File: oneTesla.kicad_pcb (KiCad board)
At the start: 2 copper layers, 106 x 106 mm, 48 parts, among them IC1 74HCT14, IC2 74HCT74, IC3 UCC37321P, IC4 UCC37321P, IC6 78L05, J1 IEC C6, J110 Jumper 110V, J2 PE/CHASSIS, P1 PRIMARIO A, P2 PRIMARIO B, Q1 FGA60N65SMD, Q2 FGA60N65SMD, T1 1:1:1, T3 1:300

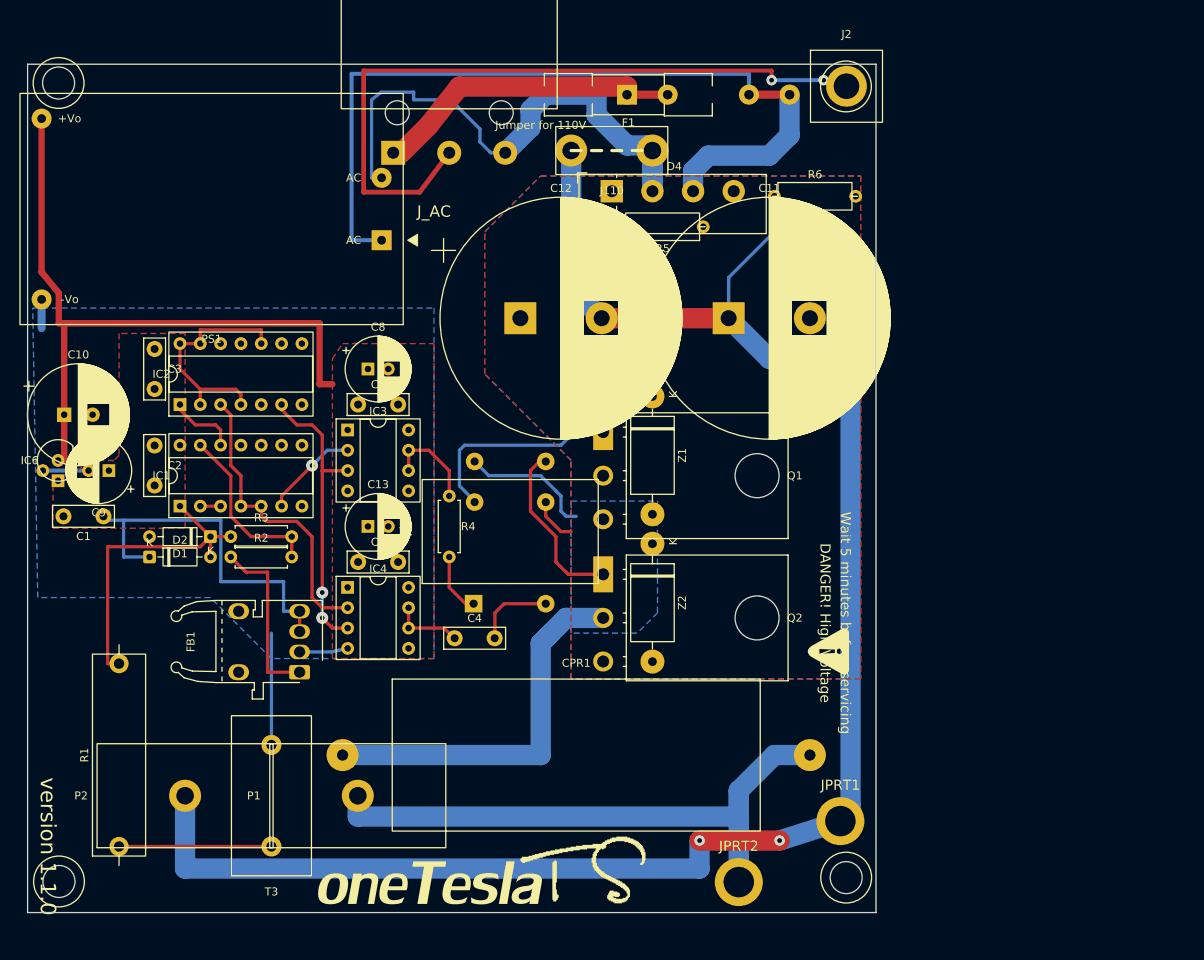
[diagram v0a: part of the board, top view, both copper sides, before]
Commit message: fix(pcb): enlarge board and space capacitor bank with verified routing
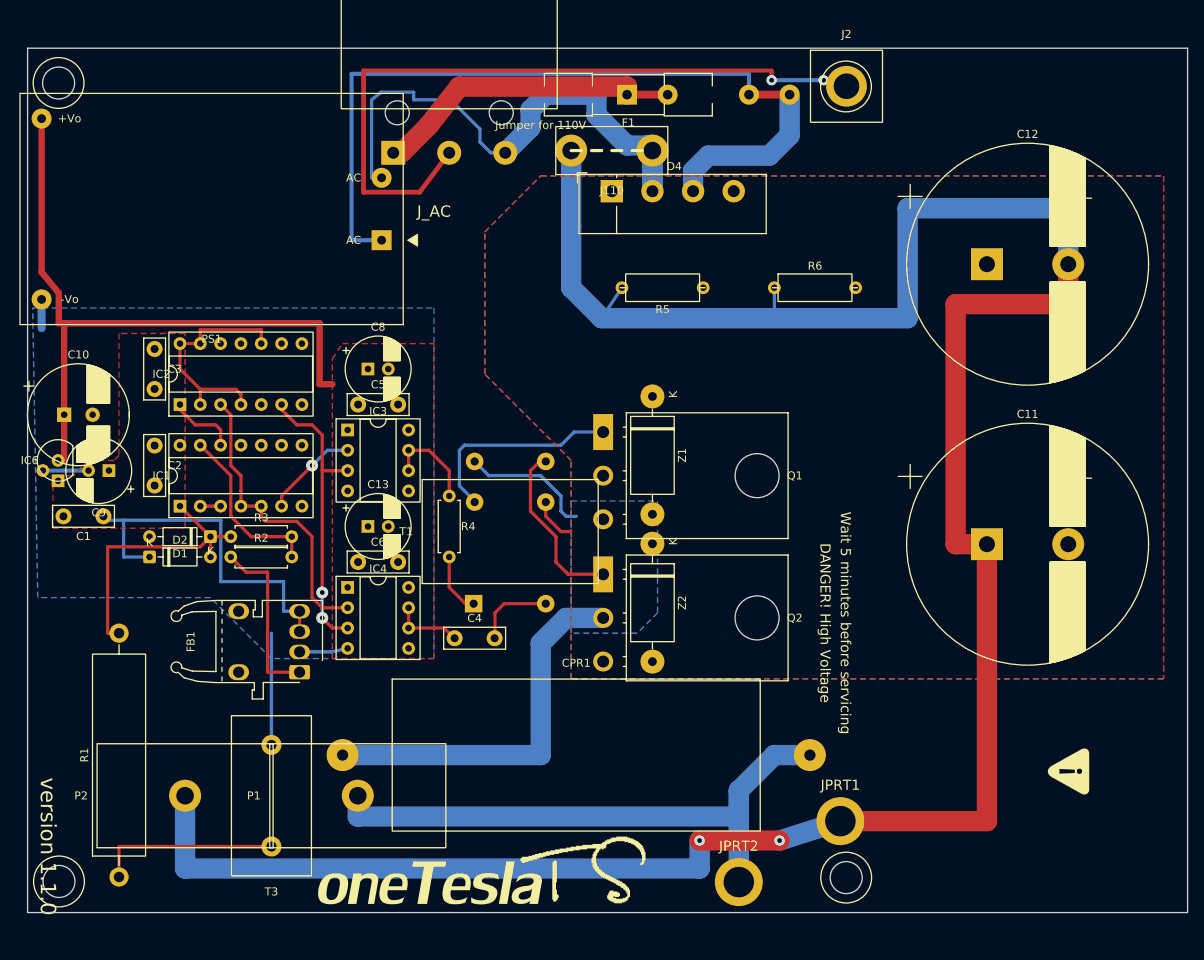
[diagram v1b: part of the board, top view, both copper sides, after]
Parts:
- R1: footprint oneTesla:R_L25_P22.86_INCOMPATIBLE -> oneTesla:R_L25_P30.48_Provisional
- moved C12 58.7 mm to (125.0, 25.0)
- moved C11 42.9 mm to (125.0, 60.0)
- moved R6 11.4 mm to (98.4, 27.9)
- moved R5 7.62 mm to (79.4, 27.9)
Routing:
- net /DC_MID: track 231.8 -> 310.8 mm
- net Net-(D1-K): track 39.9 -> 36.1 mm
- net Net-(T3-S1): track 19.1 -> 22.9 mm
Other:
- board size 106 x 106 mm -> 145 x 108 mm

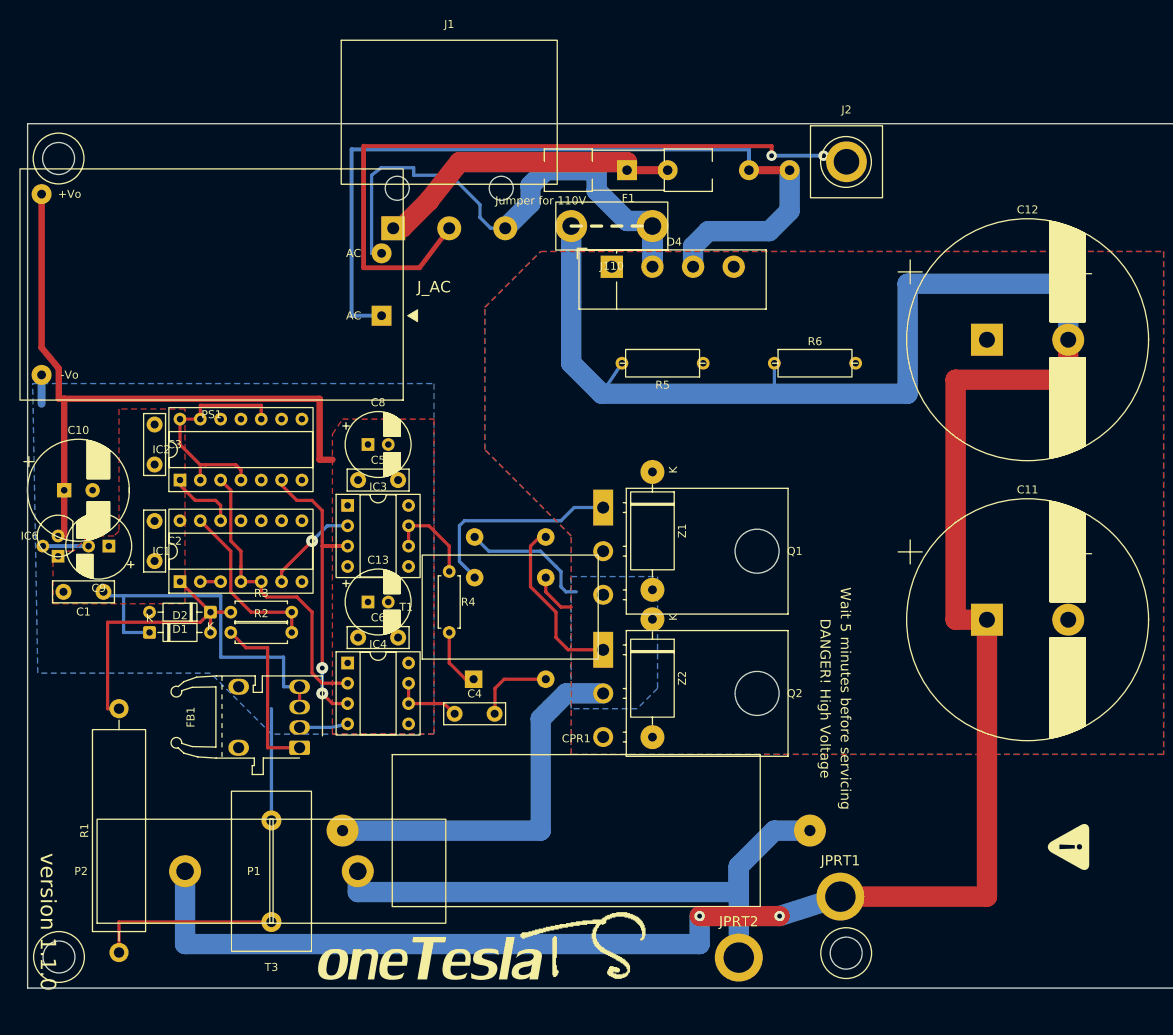
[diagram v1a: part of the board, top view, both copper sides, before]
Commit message: fix(cad): preserve geometry and document remaining DRC blockers
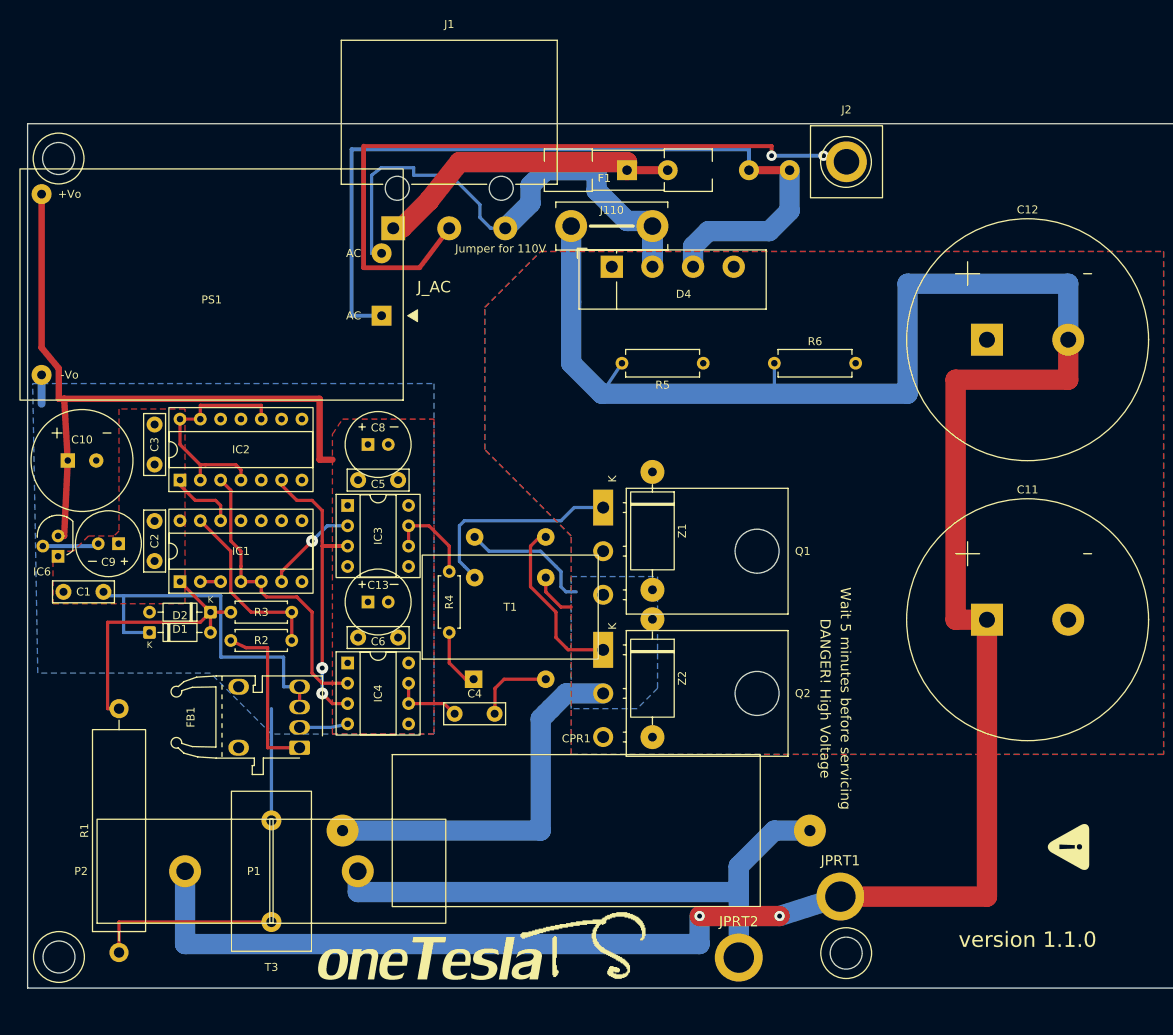
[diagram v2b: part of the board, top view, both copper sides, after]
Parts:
- Q1, Q2: footprint oneTesla:TO-3P-3_Horizontal_TabDown -> oneTesla:Q_TO3P_ImportedPads_ReviewPending
- moved C10 3.74 mm to (6.80, 40.1)
- moved C9 1.25 mm to (10.1, 50.5)
- moved R2 1.00 mm to (25.4, 62.6)
- gave numbers to parts that had none: 5
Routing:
- net GND: track 29.3 -> 30.8 mm
- net Net-(IC1-Pad13): track 21.7 -> 22.7 mm
- net /OPTICAL_OUT: track 21.9 -> 21.3 mm

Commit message: Atualiza esquema, footprints e modelos 3D dos componentes
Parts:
- removed H1, H3, H5: , oneTesla:MountingHole_D4.0
- removed H2, H4: , oneTesla:MountingHole_D5.5
- removed JPRT1, JPRT2: , oneTesla:Ring_D6_D3.81
- F1: footprint oneTesla:Fuseholder_Clip-5x20mm_Littelfuse_111_Inline_P20.00x5.00mm_D1.05mm_Horizontal -> oneTesla:Fuseholder_Idall_AS-06_5x20mm_P20.20mm_Horizontal
- IC6: value 78L05 -> L7805CV; footprint oneTesla:TO-92_Inline -> oneTesla:TO-220-3_Vertical
- J1: value IEC C6 -> 2EDGRC-5.08-02P; footprint oneTesla:IEC_C6_CONFIRMAR -> oneTesla:TerminalBlock_2EDGRC-5.08_1x02_P5.08mm_Horizontal
- P1, P2: footprint oneTesla:Primary_Terminal_M6_CONFIRMAR -> oneTesla:Primary_WirePad_D4.0mm_Drill2.2mm
- R1: footprint oneTesla:R_L25_P30.48_Provisional -> oneTesla:R_Axial_Vishay_AC05_L18.0mm_D7.5mm_P23.40mm_Horizontal
- moved C12 173.5 mm to (-45.0, 59.5)
- moved R6 157.0 mm to (-58.0, 40.9), turned to -90 degrees
- moved C11 139.2 mm to (-14.2, 59.5)
- moved F1 134.8 mm to (-47.6, 27.2)
- moved C3 126.0 mm to (-91.5, 101.5)
- moved D4 125.3 mm to (-50.4, 37.2)
- moved FB1 124.4 mm to (-77.0, 132.1)
- moved D2 120.9 mm to (-91.9, 117.8)
- moved D1 120.2 mm to (-84.2, 113.5)
- moved R2 120.1 mm to (-81.3, 117.8)
- moved R3 119.8 mm to (-81.3, 113.5)
- moved R1 119.1 mm to (-88.8, 150.7)
- moved T3 118.5 mm to (-72.5, 150.1)
- moved PS1 118.1 mm to (-73.8, 25.0), turned to -90 degrees
- moved IC2 117.4 mm to (-85.6, 95.8)
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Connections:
- IC6 pad 1: +5V -> +15V
- IC6 pad 3: +15V -> +5V
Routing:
- net /DC_MID: track 310.8 -> 0.00 mm, vias 2 -> 0
- net /AC_L_FUSED: track 103.4 -> 0.00 mm
- net /PE: track 90.7 -> 0.00 mm, vias 2 -> 0
- net +15V: track 86.1 -> 0.00 mm
- net +5V: track 75.7 -> 0.00 mm
- net Net-(CPR1-Pad2): track 75.6 -> 0.00 mm
- net /AC_N: track 70.8 -> 0.00 mm
- net /SW_NODE: track 65.0 -> 0.00 mm
- net /DRIVE_ENABLE: track 39.9 -> 0.00 mm, vias 2 -> 0
- net /AC_L: track 39.1 -> 0.00 mm
- net Net-(IC2A-C): track 37.6 -> 0.00 mm
- net Net-(D1-K): track 36.1 -> 0.00 mm
- net GND: track 30.8 -> 0.00 mm
- net /GATE_H: track 26.2 -> 0.00 mm
- net Net-(T3-S1): track 22.9 -> 0.00 mm
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- removed copper zone on F.Cu, net +15V
- removed copper zone on F.Cu, net +5V
- removed copper zone on F.Cu, net /DC_MINUS
- removed copper zone on B.Cu, net /DC_PLUS
- removed copper zone on B.Cu, net /SW_NODE
- removed copper zone on B.Cu, net GND
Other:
- board outline removed
- board text removed: "DANGER! High Voltage"
- board text removed: "J110"
- board text removed: "J_AC"
- board text removed: "Jumper for 110V"
- board text removed: "Replace with 250V 4A fuse only"
- board text removed: "Wait 5 minutes before servicing"
- board text removed: "version 1.1.0"

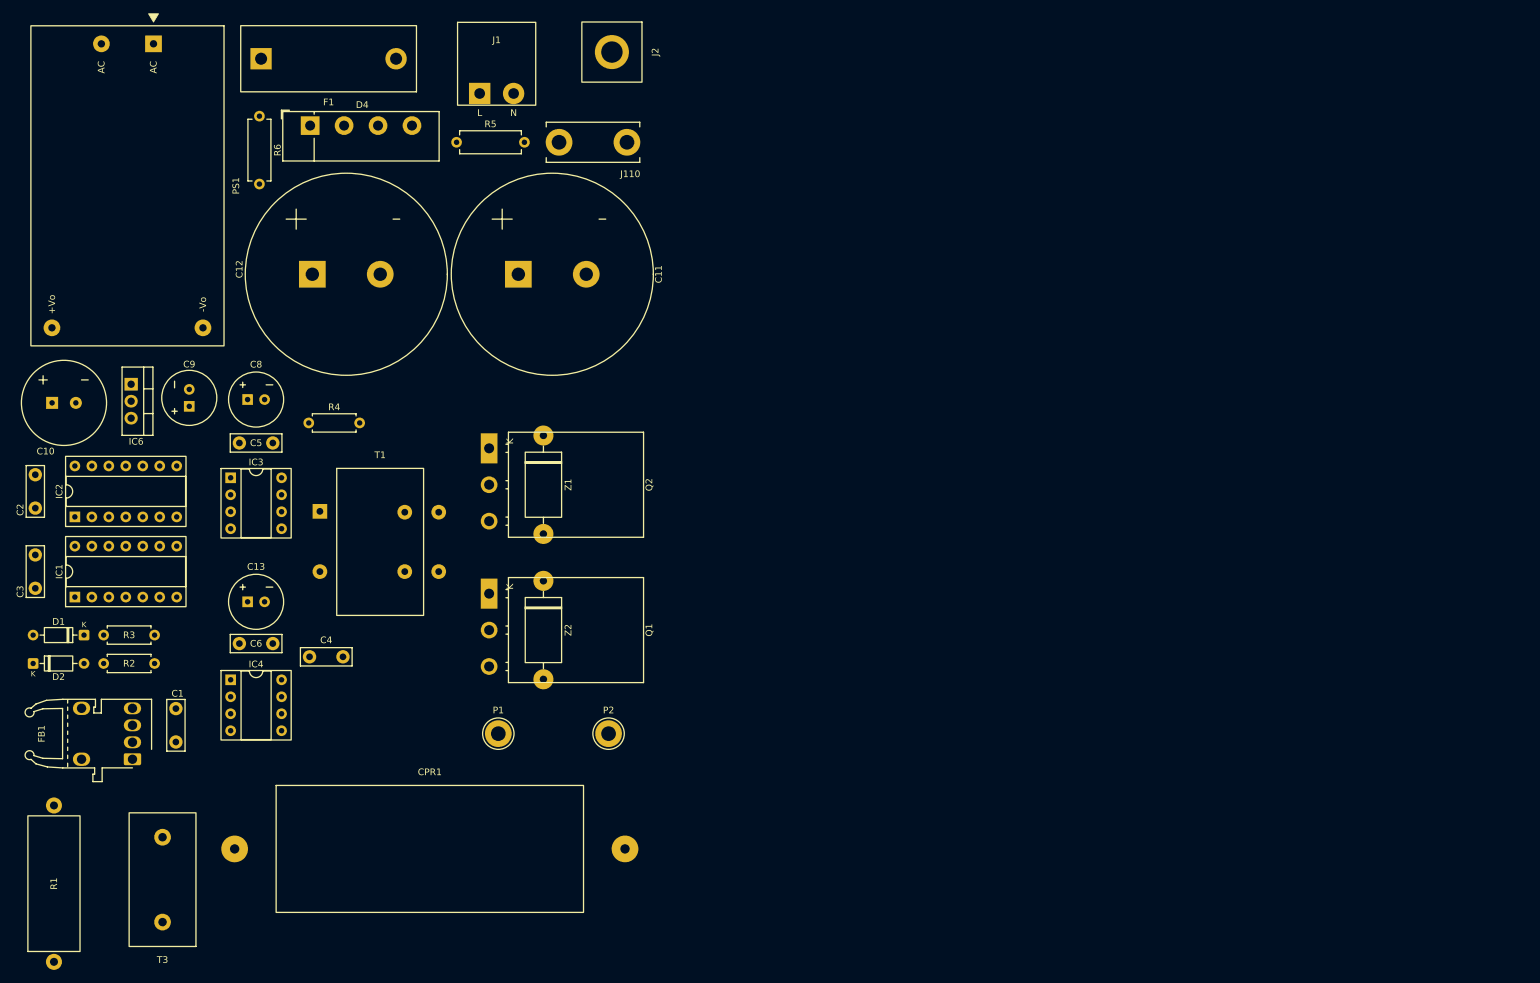
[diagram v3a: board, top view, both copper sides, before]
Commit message: cad(board): converte ICs e passivos para SMD e reduz contorno para 100x100mm
- Esquema: IC1/IC2 SOIC-14, desacoplamento 0805, R5/R6 2512,
  D1/D2 1N4148WS SOD-323, IC6 DPAK, C8/C10/C13 CP_Elec_8x10, C9 1210,
  R1 vertical AC05, R2/R3 1206, R4 DIN0207 THT
- PCB: reposicionamento e roteamento, contorno (31,375;27,05)-(131,375;127,05)mm
- Valores de referência ocultos na PCB
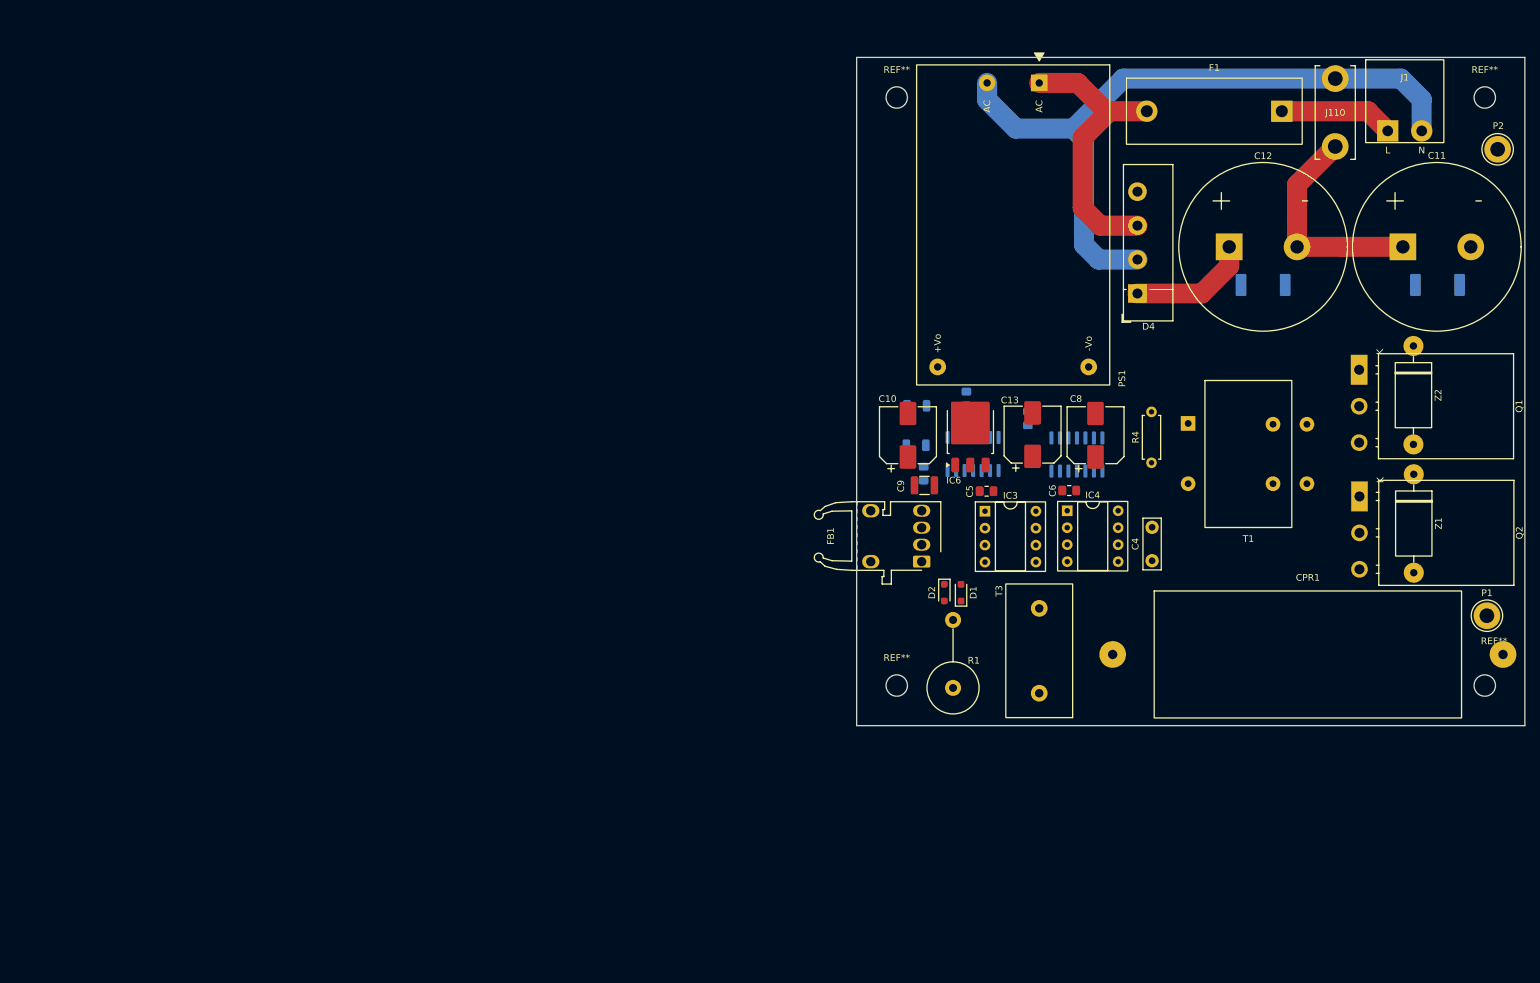
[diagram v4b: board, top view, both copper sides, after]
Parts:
- removed J2: PE/CHASSIS, oneTesla:Chassis_PE_M3
- added REF**: MountingHole_3.2mm_M3, MountingHole:MountingHole_3.2mm_M3, F.Cu at (125.4, 33.0)
- added REF**: MountingHole_3.2mm_M3, MountingHole:MountingHole_3.2mm_M3, F.Cu at (37.4, 33.0)
- added REF**: MountingHole_3.2mm_M3, MountingHole:MountingHole_3.2mm_M3, F.Cu at (125.4, 121.0)
- added REF**: MountingHole_3.2mm_M3, MountingHole:MountingHole_3.2mm_M3, F.Cu at (37.4, 121.0)
- C1, C2, C3: footprint oneTesla:C_Disc_D7.5mm_W2.5mm_P5.00mm -> oneTesla:C_0805_2012Metric_Pad1.18x1.45mm_HandSolder; moved to B.Cu
- C10: value 680u 35V -> 100u 35V; footprint oneTesla:CP_D12.5_P3.556_ReviewPending -> oneTesla:CP_Elec_8x10
- C11, C12: footprint oneTesla:CP_D30_P10.16_ReviewPending -> oneTesla:CP_D25_H45_P10.16_ReviewPending
- C13, C8: value 100u 25V -> 100u 35V; footprint oneTesla:CP_D8_P2.54_ReviewPending -> oneTesla:CP_Elec_8x10
- C5, C6: footprint oneTesla:C_Disc_D7.5mm_W2.5mm_P5.00mm -> oneTesla:C_0805_2012Metric_Pad1.18x1.45mm_HandSolder
- C9: value 100u 10V -> 10u 100V; footprint oneTesla:CP_D8_P2.54_ReviewPending -> oneTesla:C_1210_3225Metric
- D1, D2: value 1N4148 -> 1N4148WS; footprint oneTesla:D_DO-35_SOD27_P7.62mm_Horizontal -> oneTesla:D_SOD-323_HandSoldering
- IC1, IC2: footprint oneTesla:DIP-14_W7.62mm_Socket_LongPads -> oneTesla:SOIC-14_3.9x8.7mm_P1.27mm; moved to B.Cu
- IC6: value L7805CV -> MC7805BDTRKG; footprint oneTesla:TO-220-3_Vertical -> oneTesla:TO-252-3_TabPin2
- R1: footprint oneTesla:R_Axial_Vishay_AC05_L18.0mm_D7.5mm_P23.40mm_Horizontal -> oneTesla:R_Axial_Vishay_AC05_L18.0mm_D7.5mm_P10.16mm_Vertical
- R2, R3: footprint oneTesla:R_Axial_DIN0207_L6.3mm_D2.5mm_P7.62mm_Horizontal -> oneTesla:R_1206_3216Metric; moved to B.Cu
- R5, R6: footprint oneTesla:R_L9_P10.16_ReviewPending -> oneTesla:R_Uniroyal_HV12_2512_P6.60mm; moved to B.Cu
- moved P2 159.2 mm to (127.3, 40.8)
- moved R6 151.5 mm to (92.2, 61.1), turned to 0 degrees
- moved IC2 150.3 mm to (64.3, 86.5)
- moved P1 149.0 mm to (125.7, 110.6)
- moved C2 148.8 mm to (57.0, 81.1)
- moved R5 143.3 mm to (118.3, 61.1)
- moved C3 141.3 mm to (47.8, 78.1)
- moved R1 138.9 mm to (45.8, 116.3)
- moved C12 137.3 mm to (92.2, 55.4)
- moved D2 136.8 mm to (44.5, 107.2), turned to -90 degrees
- moved IC1 136.1 mm to (48.8, 86.4)
- moved J1 136.0 mm to (110.9, 38.0)
- moved T3 135.6 mm to (58.7, 115.8)
- moved Z2 134.9 mm to (114.7, 77.6)
- moved CPR1 134.6 mm to (98.9, 116.4)
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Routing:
- net /AC_N: track 0.00 -> 105.4 mm
- net /AC_L_FUSED: track 0.00 -> 43.1 mm
- net /DC_MID: track 0.00 -> 33.4 mm
- net /DC_PLUS: track 0.00 -> 18.3 mm
- net /AC_L: track 0.00 -> 17.1 mm
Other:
- board outline added: 100 x 100 mm
